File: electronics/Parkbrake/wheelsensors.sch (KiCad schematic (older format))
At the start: 52 parts, among them Q33 NX3008CBKS, U31 MAX232, U32 MAX232, U33 NCV1124, U34 NCV1124, U35 74LVC08

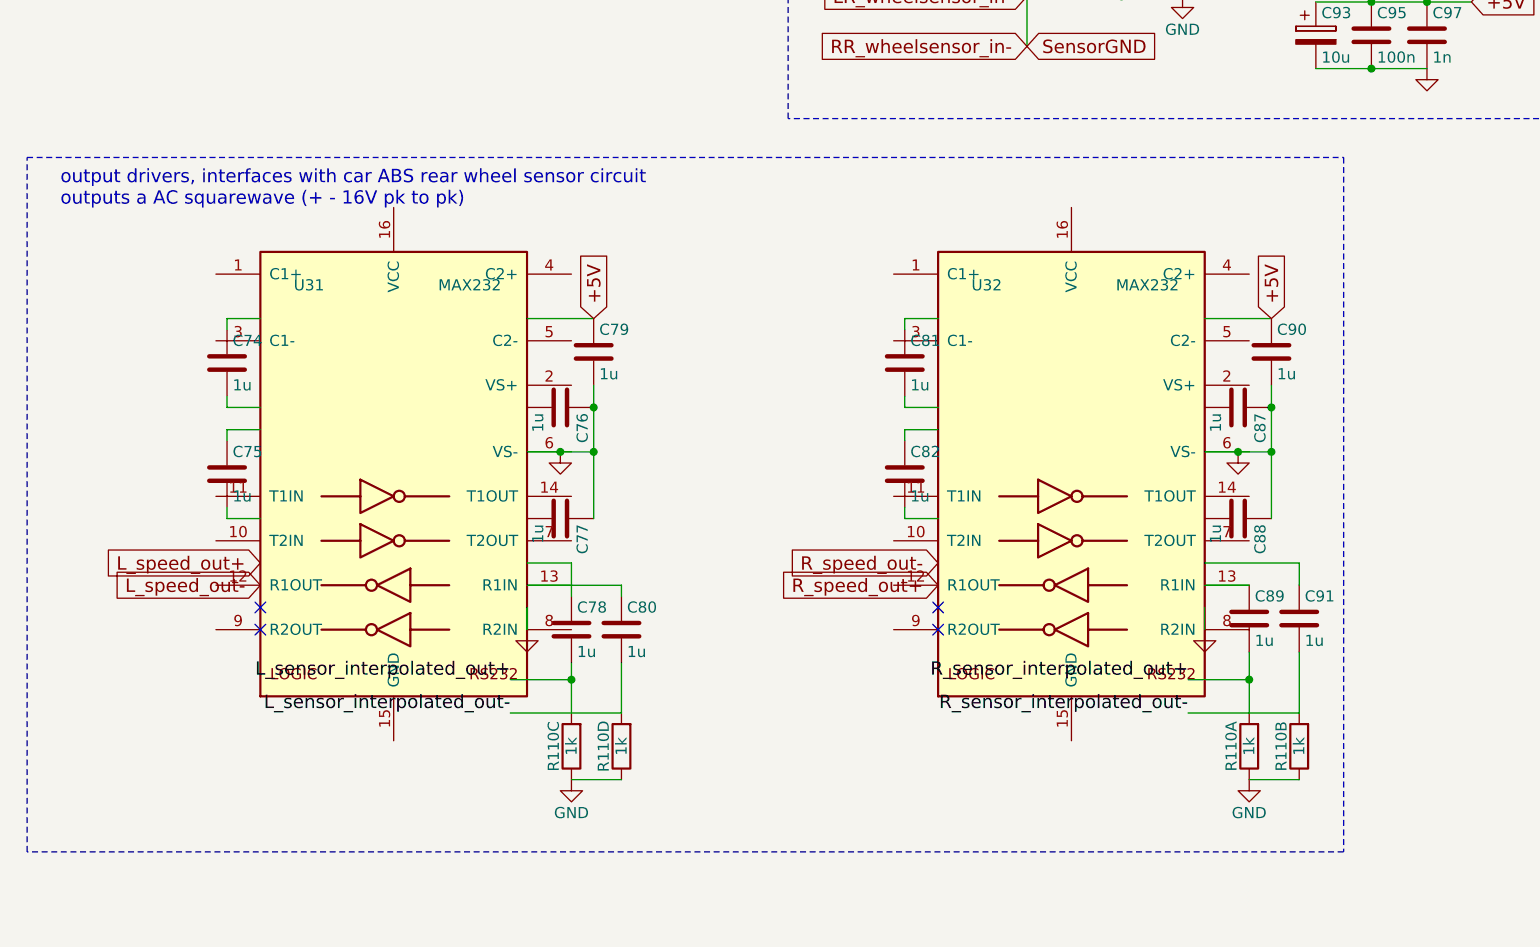
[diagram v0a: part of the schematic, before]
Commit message: minor tweaks to pcb, had a cap on wrong polarity
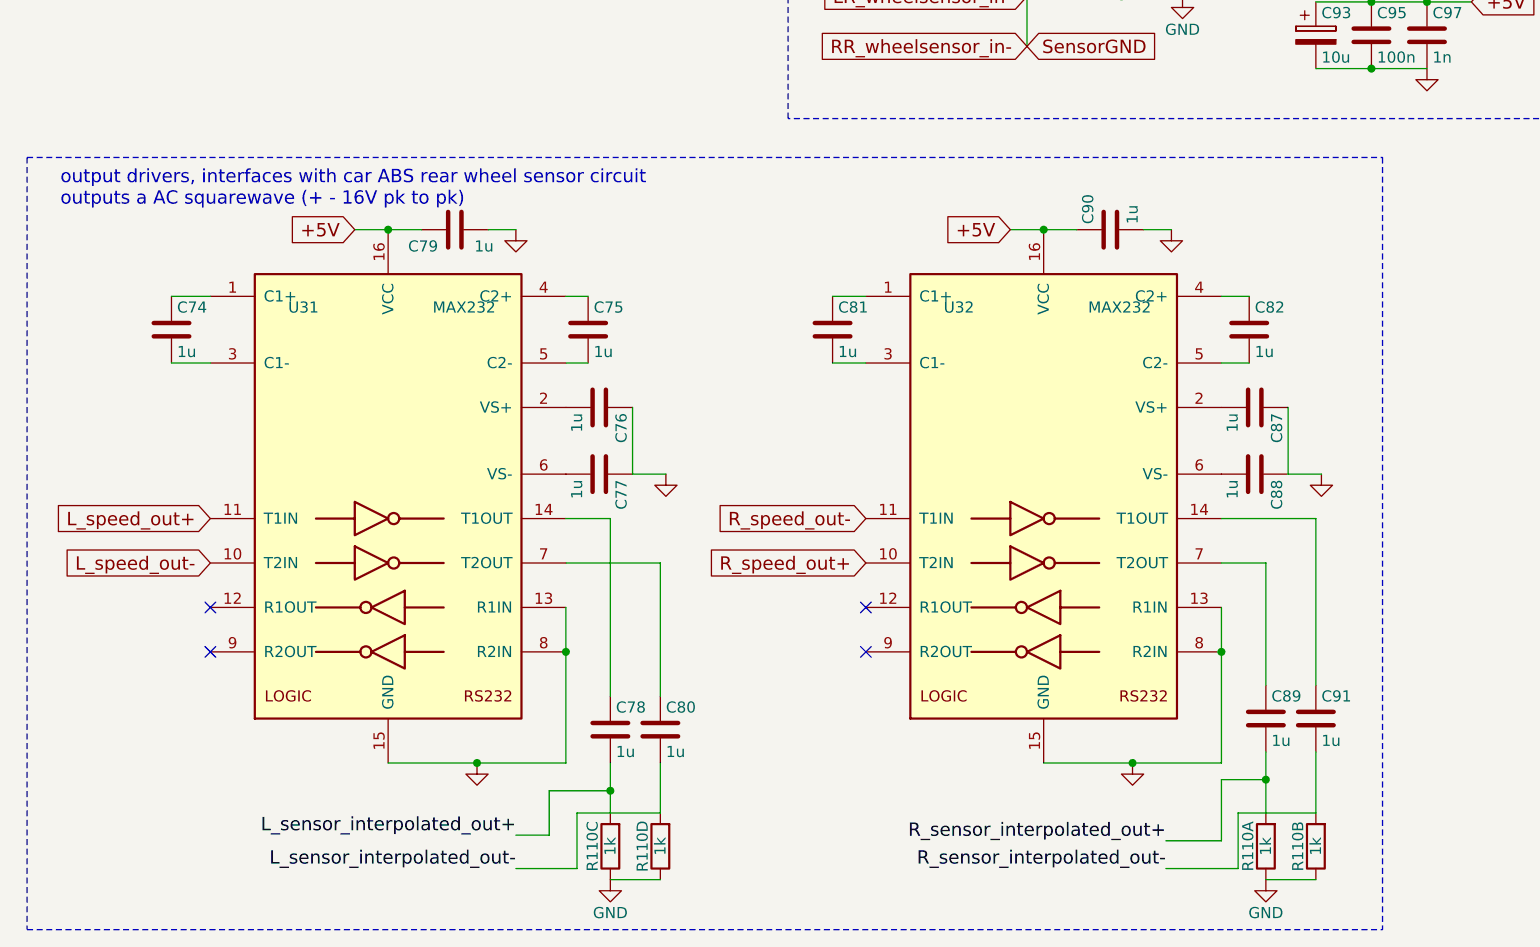
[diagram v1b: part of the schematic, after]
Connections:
- wire segments 90 -> 95
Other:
- moved on the sheet: C74, C75, C76, C77, C78, C79, C80, C81, C82, C87, C88, C89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
